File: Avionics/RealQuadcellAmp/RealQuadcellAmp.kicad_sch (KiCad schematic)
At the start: 73 parts, among them J1 Screw_Terminal_01x02, J2 Conn_01x04_Pin, U1 OPA1642AID, U2 OPA1642AID, U3 OPA1642AID, U4 OPA1642AID, U6 L78L33_SOT89

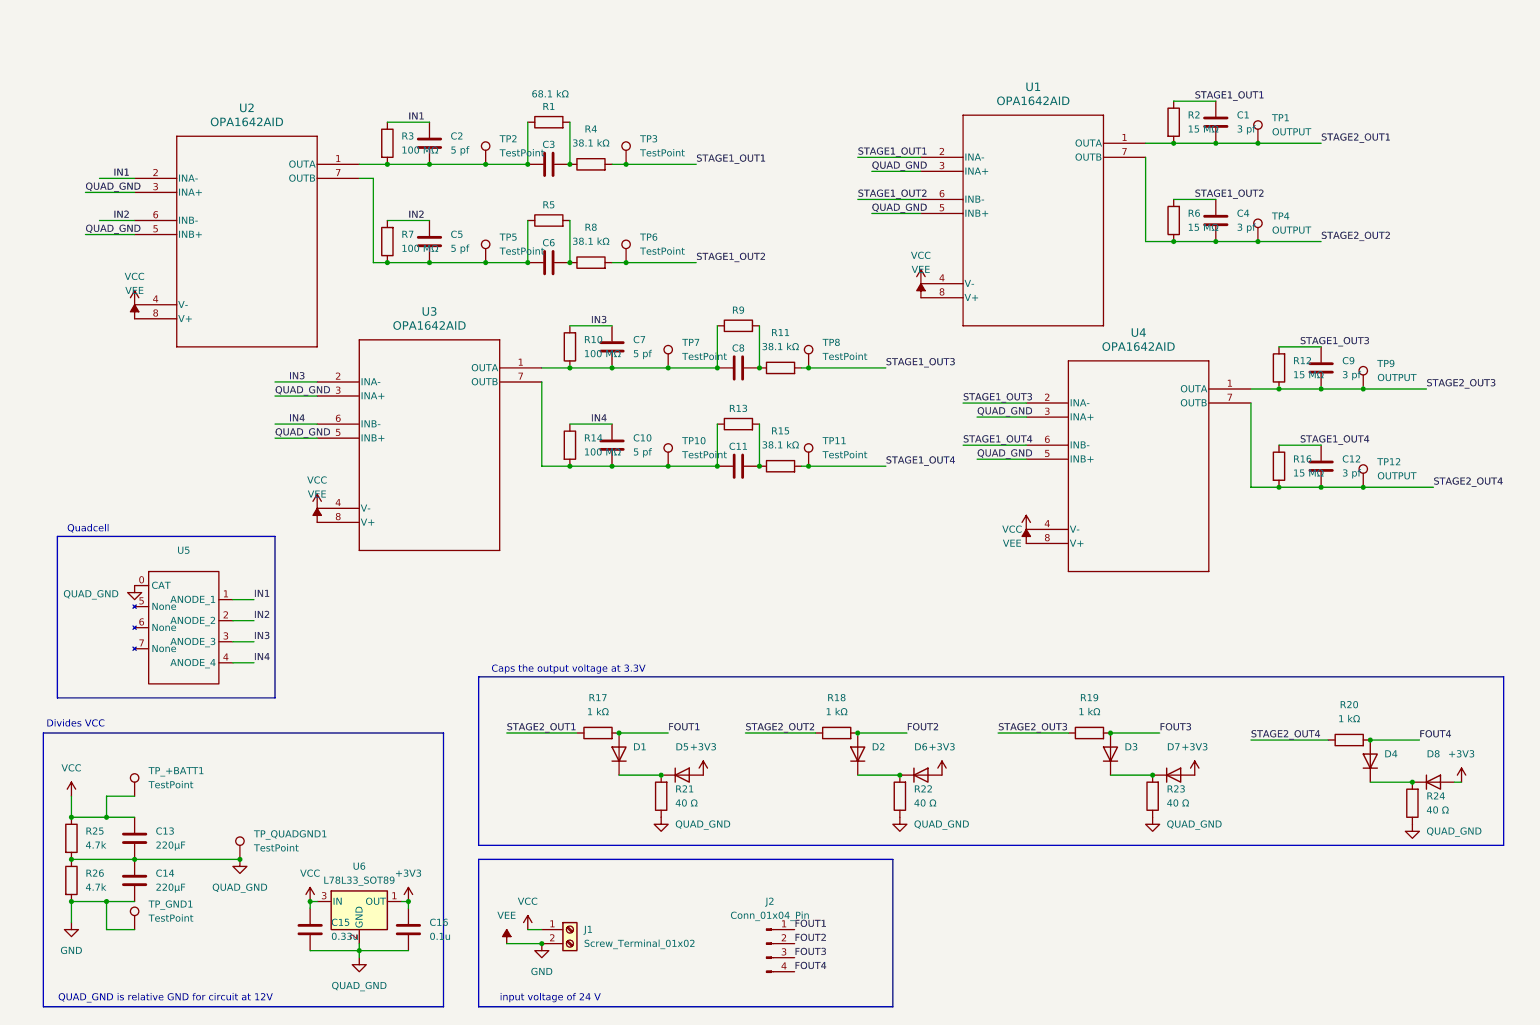
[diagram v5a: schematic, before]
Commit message: added intermediary connectors and voltage caps after stage 1
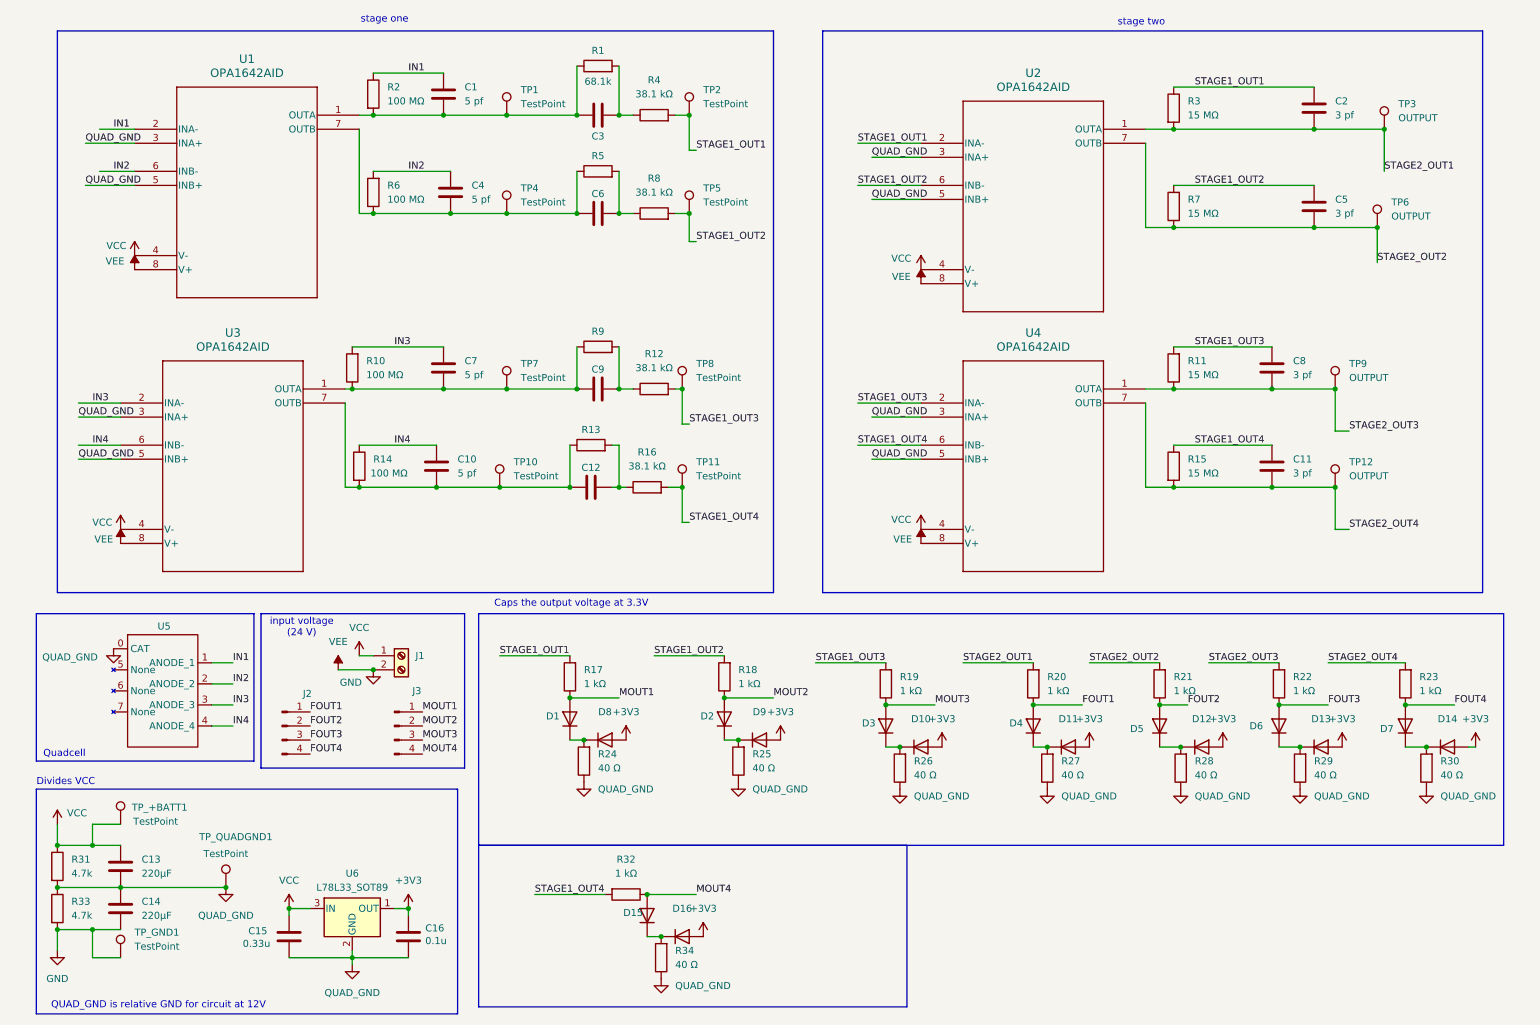
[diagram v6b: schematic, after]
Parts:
- added D1, D10, D15, D16, D2, D3, D8, D9: ~, Diode_SMD:D_0805_2012Metric_Pad1.15x1.40mm_HandSolder, symbol Diode:1N4001
- added J3: Conn_01x04_Pin, Connector_PinHeader_2.54mm:PinHeader_1x04_P2.54mm_Vertical, symbol Connector:Conn_01x04_Pin
- added R17, R18, R19, R32: 1 kΩ, Resistor_SMD:R_0805_2012Metric_Pad1.20x1.40mm_HandSolder, symbol Device:R
- added R24, R25, R26, R34: 40 Ω, Resistor_SMD:R_0805_2012Metric_Pad1.20x1.40mm_HandSolder, symbol Device:R
- R1: value 68.1 kΩ -> 68.1k
- renumbered C2 to C1, C12 to C11, C11 to C12, C1 to C2, C5 to C4, C4 to C5, C9 to C8, C8 to C9, D5 to D11, D6 to D12, D7 to D13, D8 to D14, D1 to D4, D2 to D5, D3 to D6, D4 to D7, R12 to R11, R11 to R12, R16 to R15, R15 to R16, R3 to R2, R17 to R20, R18 to R21, R19 to R22, R20 to R23, R21 to R27, R22 to R28, R23 to R29, R2 to R3, R24 to R30, R25 to R31, R26 to R33, R7 to R6, R6 to R7, TP2 to TP1, TP3 to TP2, TP1 to TP3, TP5 to TP4, TP6 to TP5, TP4 to TP6, U2 to U1, U1 to U2
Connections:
- net +3V3: now also D10.2 (A), D16.2 (A), D8.2 (A), D9.2 (A)
- net FOUT1: now also R20.1; no longer R20.2
- net FOUT2: now also R21.1; no longer R21.2
- net FOUT3: now also R22.1; no longer R22.2
- net FOUT4: now also R23.1; no longer R23.2
- net QUAD_GND: now also R24.1, R25.1, R26.1, R34.1
- net STAGE1_OUT1: now also R17.2
- net STAGE1_OUT2: now also R18.2
- net STAGE1_OUT3: now also R19.2
- net STAGE1_OUT4: now also R32.2
- net STAGE2_OUT1: now also R20.2; no longer R20.1
- net STAGE2_OUT2: now also R21.2; no longer R21.1
- net STAGE2_OUT3: now also R22.2; no longer R22.1
- net STAGE2_OUT4: now also R23.2; no longer R23.1
- new net: D10.1 (K), D3.1 (K), R26.2
- new net: D15.1 (K), D16.1 (K), R34.2
- new net: D1.1 (K), D8.1 (K), R24.2
- new net: D2.1 (K), D9.1 (K), R25.2
- new net MOUT1: D1.2 (A), J3.1 (Pin_1), R17.1
- new net MOUT2: D2.2 (A), J3.2 (Pin_2), R18.1
- new net MOUT3: D3.2 (A), J3.3 (Pin_3), R19.1
- new net MOUT4: D15.2 (A), J3.4 (Pin_4), R32.1
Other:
- note added: "input voltage (24 V)"
- note added: "stage one"
- note added: "stage two"
- note removed: "input voltage of 24 V"
- moved on the sheet: C1, C10, C11, C12, C13, C14, C15, C16, C2, C3, C4, C5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

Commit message: changed footprints of large caps
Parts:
- C13, C14: footprint Capacitor_SMD:C_0805_2012Metric_Pad1.18x1.45mm_HandSolder -> Capacitor_THT:CP_Radial_D5.0mm_P2.00mm
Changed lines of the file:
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@@
 			)
 		)
-		(property "Footprint" "Capacitor_SMD:C_0805_2012Metric_Pad1.18x1.45mm_HandSolder"
+		(property "Footprint" "Capacitor_THT:CP_Radial_D5.0mm_P2.00mm"
 			(at 30.1752 171.45 0)
 			(effects
@@
 			)
 		)
-		(property "Footprint" "Capacitor_SMD:C_0805_2012Metric_Pad1.18x1.45mm_HandSolder"
+		(property "Footprint" "Capacitor_THT:CP_Radial_D5.0mm_P2.00mm"
 			(at 30.1752 179.07 0)
 			(effects
